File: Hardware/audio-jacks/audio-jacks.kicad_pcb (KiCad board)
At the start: 4 copper layers, 48 x 36 mm, 30 parts, among them J1 Barrel_Jack_Switch, J2 BM28B0.6-24DS/2, J3 AudioJack2_SwitchT, J4 AudioJack2_SwitchT, J5 Conn_01x12_MountingPin, U1 TLV76750DRVx, U2 OPA365xxDBV, U3 TLV76733DRVx

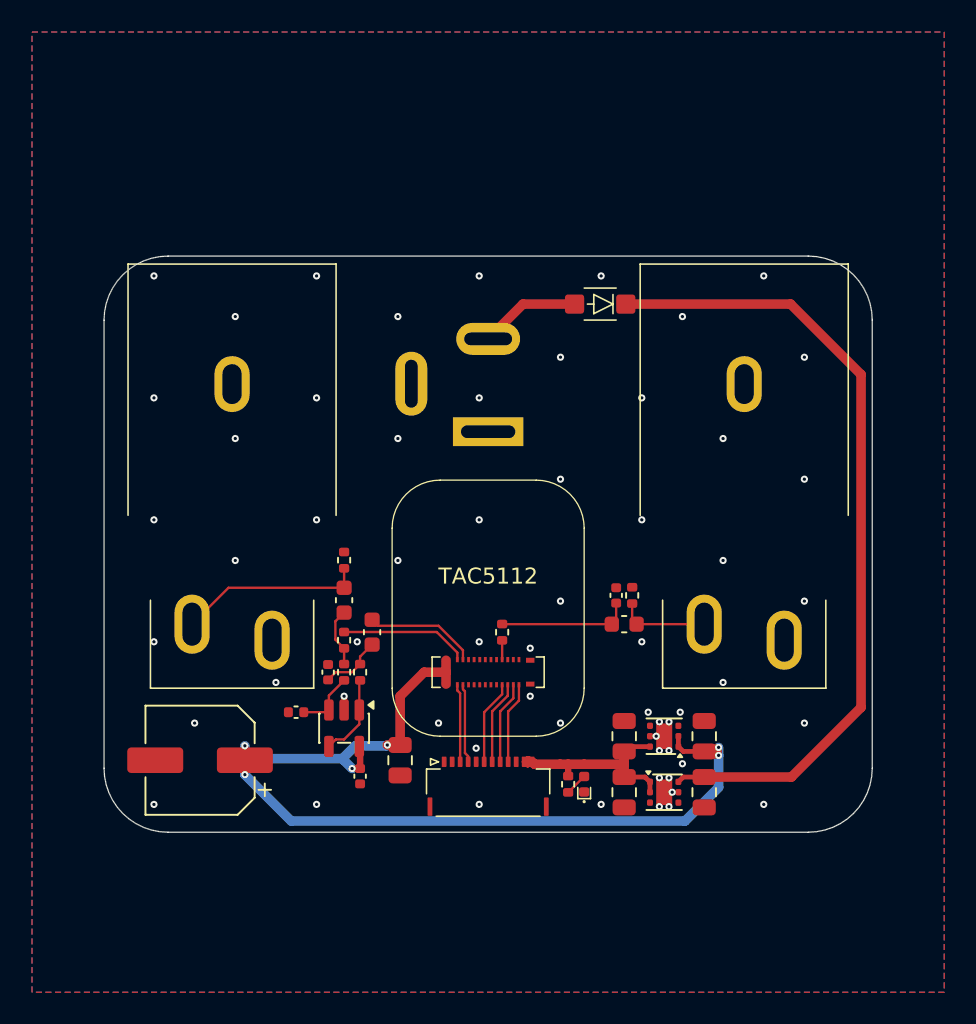
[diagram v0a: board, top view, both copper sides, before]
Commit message: Update the audio-jacks board
The old audio jack board actually works quite well, and I've used the
same board now in a few different form factors, which is a good sign.

However, I do want to try doing a stereo board, and the old one was
using mono audio jacks.  That was partly historical, but also partly a
size issue: the particular mono jacks I use are just smaller than the
stereo jacks I have.  And there are obviously fewer components in the
mono setup.

However, exactly because the form factor has worked fairly well, I felt
like I could avoid the whole separate TAC5112 board that I had used with
the (quite nice and compact, but a bit of a pain to route out of) BM28
connector.

The TAC5112 is actually easier to route on its own than using the codec
board - the advantage of that separate board was that I could then do
various test variations using it, and re-use the CODEC board when those
variations failed.  Which they certainly have done - I've tried a lot of
different form factors.

So now that I feel more comfortable with the form factor and think it
works, I might as well put the codec chip directly on the board, which
makes things easier and more compact.

As a result it's not a problem to fit the larger dual op-amp for
buffering the input signal, and the other extra analog components.

There are a few other changes than just switching to stereo jacks and a
dual op-amp.  The big one is that this uses the TAC5242 instead of the
TAC5112.  It doesn't do i2c for control, it's set up with hardware
strapping of five control pins instead.  I liked having i2c for testing
things, but again, now I basically know what my setup is.

The FFC cable still brings in i2c from the controller board, but now
it's only connected to the EEPROM.  And since that's the only thing it
is used for, I decided to upgrade it a bit - from a 2kbit EEPROM to a
64kbit one.

The 2kbit one worked fine, but I didn't expect to have as much config
data as I do.  For all the best kinds of reasons: t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
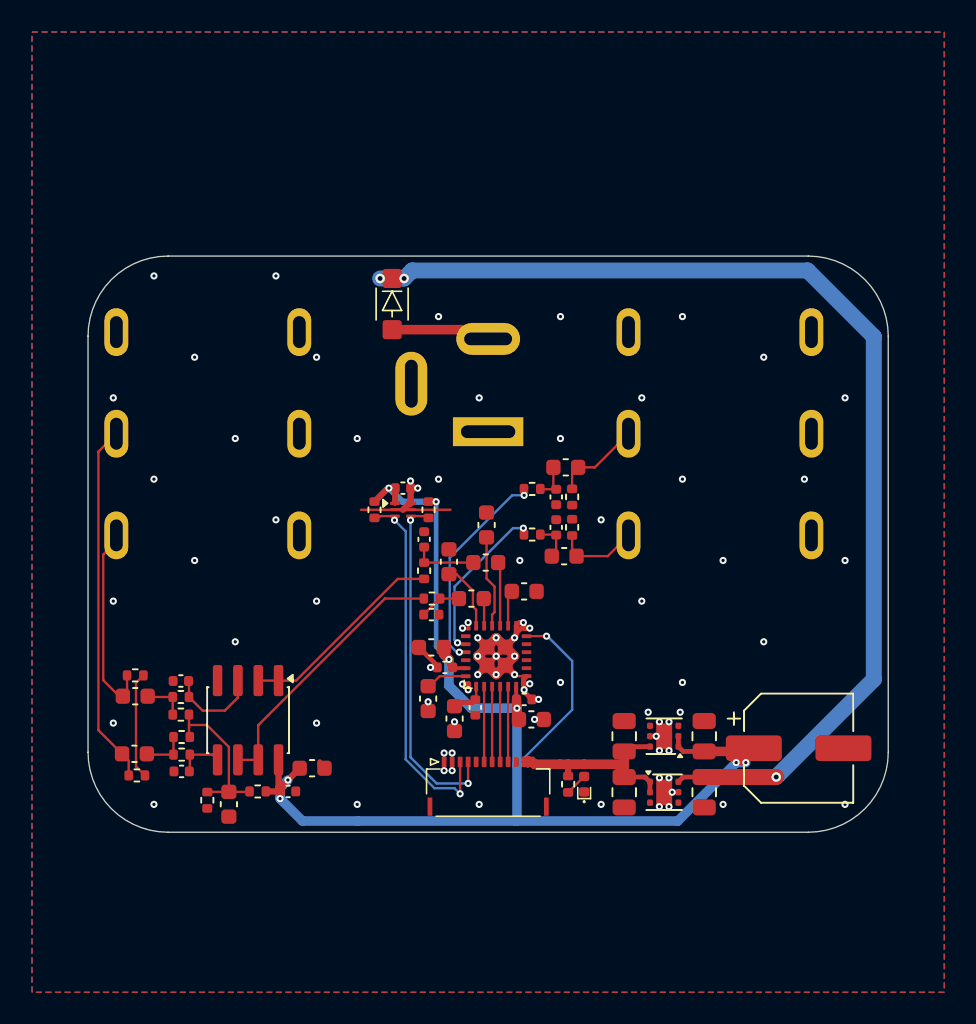
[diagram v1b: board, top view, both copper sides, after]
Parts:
- removed the C10 at (94.5, 131.5)
- removed the J4 at (116.0, 108.0)
- added C13: 1uF, Capacitor_SMD:C_0603_1608Metric, F.Cu at (83.8, 134.2)
- added C16: 1uF, Capacitor_SMD:C_0603_1608Metric, F.Cu at (96.2, 127.7)
- added C17: 1uF, Capacitor_SMD:C_0603_1608Metric, F.Cu at (102.2, 121.0)
- added C18: 1uF, Capacitor_SMD:C_0603_1608Metric, F.Cu at (77.9, 131.1)
- added C19: 1uF, Capacitor_SMD:C_0603_1608Metric, F.Cu at (99.0, 121.4)
- added C20: 150pF, Capacitor_SMD:C_0402_1005Metric, F.Cu at (80.8, 132.2)
- added C21: 2.2nF, Capacitor_SMD:C_0402_1005Metric, F.Cu at (96.5, 122.4)
- added C22: 1uF, Capacitor_SMD:C_0603_1608Metric, F.Cu at (104.8, 113.2)
- added C23: 2.2nF, Capacitor_SMD:C_0402_1005Metric, F.Cu at (104.2, 115.0)
- added C24: 10uF, Capacitor_SMD:C_0603_1608Metric, F.Cu at (102.7, 128.9)
- added C25: 10uF, Capacitor_SMD:C_0603_1608Metric, F.Cu at (96.5, 124.5)
- added C26: 10uF, Capacitor_SMD:C_0603_1608Metric, F.Cu at (89.0, 132.0)
- added C27: 0.1uF, Capacitor_SMD:C_0402_1005Metric, F.Cu at (102.2, 127.7)
- added C28: 0.1uF, Capacitor_SMD:C_0402_1005Metric, F.Cu at (97.3, 125.7)
- added C29: 10uF, Capacitor_SMD:C_0603_1608Metric, F.Cu at (97.9, 128.9)
- added C3: 1uF, Capacitor_SMD:C_0603_1608Metric, F.Cu at (99.9, 116.8)
- added C30: 0.1uF, Capacitor_SMD:C_0402_1005Metric, F.Cu at (99.2, 128.2)
- added C31: 0.1uF, Capacitor_SMD:C_0402_1005Metric, F.Cu at (94.7, 114.5)
- added C4: 1uF, Capacitor_SMD:C_0603_1608Metric, F.Cu at (97.5, 119.1)
- added R11: 1k, Resistor_SMD:R_0402_1005Metric, F.Cu at (80.8, 131.2)
- added R12: 1k, Resistor_SMD:R_0402_1005Metric, F.Cu at (96.5, 121.4)
- added R13: 1MEG, Resistor_SMD:R_0402_1005Metric, F.Cu at (78.0, 132.4)
- added R14: 1k, Resistor_SMD:R_0402_1005Metric, F.Cu at (102.8, 114.5)
- added R15: 1MEG, Resistor_SMD:R_0402_1005Metric, F.Cu at (105.2, 115.0)
- added R16: 4k7, Resistor_SMD:R_0402_1005Metric, F.Cu at (92.9, 115.8)
- added R17: 4k7, Resistor_SMD:R_0402_1005Metric, F.Cu at (96.3, 115.8)
- added R6: 1MEG, Resistor_SMD:R_0402_1005Metric, F.Cu at (85.6, 133.4)
- added R7: 1MEG, Resistor_SMD:R_0402_1005Metric, F.Cu at (82.5, 134.0)
- added R8: 1MEG, Resistor_SMD:R_0402_1005Metric, F.Cu at (80.8, 130.1)
- added U4: TAC5242, Mylib:TAC5242, F.Cu at (100.5, 125.0)
- added U5: M24C64-FMH6TG, Mylib:UFDFPN5, F.Cu at (94.7, 115.8)
- J2: value BM28B0.6-24DS/2 -> AudioJack3_SwitchTR; footprint Mylib:BM28B0.6-24DS -> Mylib:NRJ6HM-1-PRE
- J3: value AudioJack2_SwitchT -> AudioJack3_SwitchTR; footprint Mylib:CK-6.35-no-NPTH -> Mylib:NRJ6HM-1-PRE
- R1: value 1k / thin-film -> 1k
- R10: renamed from R7; value 1MEG / thin-film -> 1MEG
- R2: renamed from R5; value 1k / thin-film -> 1k
- R3: renamed from R2; value 1k / thin-film -> 1k
- R4: renamed from R3; value 1MEG / thin-film -> 1MEG
- R5: renamed from R4; value 1MEG / thin-film -> 1MEG
- R9: renamed from R6; value 1k / thin-film -> 1k
- U2: value OPA365xxDBV -> OPA2365AIDR; footprint Package_TO_SOT_SMD:SOT-23-5 -> Package_SO:SOIC-8_3.9x4.9mm_P1.27mm
- moved C6 37.4 mm to (119.4, 130.8), turned to 0 degrees
- moved J3 33.0 mm to (116.0, 100.0), turned to 90 degrees
- moved J2 30.5 mm to (84.0, 100.0), turned to 90 degrees
- moved R4 14.9 mm to (78.0, 126.2), turned to 0 degrees
- moved C7 14.4 mm to (78.0, 127.5), turned to 0 degrees
- moved D1 13.0 mm to (94.0, 103.0), turned to -90 degrees
- moved R5 11.2 mm to (80.8, 128.7), turned to 180 degrees
- moved R1 10.3 mm to (80.8, 127.5), turned to 0 degrees
- moved C12 10.2 mm to (96.0, 117.7)
- moved C8 8.33 mm to (99.8, 119.2), turned to 0 degrees
- moved R3 7.50 mm to (96.0, 119.7)
- moved C11 7.46 mm to (80.8, 126.5)
- moved R9 6.38 mm to (102.8, 117.4), turned to 0 degrees
- moved U2 6.02 mm to (85.0, 129.0)
- moved C14 5.67 mm to (104.8, 118.8)
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- renumbered C2 to C1, C9 to C10, C6 to C11, C7 to C12, C12 to C14, C13 to C15, C3 to C2, C1 to C5, C11 to C6, C4 to C7, C5 to C8, C8 to C9, J5 to J4
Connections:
- C14 pad 2: OUT^{CONN} -> OUT^{LEFT}
- C7 pad 1: IN^{CONN} -> IN^{LEFT}
- J3 pad T: IN^{CONN} -> OUT^{LEFT}
- J3 pad TN: GND -> unconnected-(J3-PadTN)
- J4 pad 3: /TAC_SDA -> /SDA
- J4 pad 4: /TAC_SCL -> /SCL
- R10 pad 1: OUT^{CONN} -> OUT^{LEFT}
- R3 pad 1: Net-(U2--) -> Net-(U2A--)
- R4 pad 1: IN^{CONN} -> IN^{LEFT}
- R5 pad 1: /MICBIAS -> Net-(C13-Pad2)
- U2 pad 1: Net-(U2--) -> Net-(U2A--)
- U2 pad 2: GND -> Net-(U2A--)
- U2 pad 4: Net-(U2--) -> GND
- U2 pad 5: +3V3 -> Net-(U2B-+)
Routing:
- net GND: track 0.86 -> 36.5 mm, vias 60 -> 80
- net /SDA: track 0.00 -> 23.1 mm, vias 0 -> 2
- net IN^{RIGHT}: track 0.00 -> 22.6 mm
- net /SCL: track 0.00 -> 21.9 mm, vias 0 -> 2
- net +8V: track 50.7 -> 70.5 mm, vias 0 -> 3
- net +3V3: track 72.0 -> 91.3 mm, vias 6 -> 9
- net Net-(U2B--): track 0.00 -> 17.1 mm
- net /OUT2P: track 0.00 -> 13.3 mm, vias 0 -> 2
- net Net-(U2A--): track 0.00 -> 13.0 mm
- net IN^{LEFT}: track 0.00 -> 12.4 mm
- net IN^{CONN}: track 11.7 -> 0.00 mm
- net Net-(C13-Pad2): track 0.00 -> 9.94 mm
- net /OUT1P: track 1.20 -> 10.4 mm, vias 0 -> 2
- net Net-(C14-Pad1): track 8.29 -> 2.44 mm
- net /MICBIAS: track 8.05 -> 2.24 mm
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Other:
- board size 48 x 36 mm -> 50 x 36 mm
- board text removed: "TAC5112"
